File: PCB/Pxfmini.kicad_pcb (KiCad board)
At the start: 2 copper layers, 9 parts, among them P0 Raspberry pi GPIO, P1 MPU9250, P2 MS5611, P3 PCA9685, P4 PCA9685_2, P5 UART, P6 RC INPUT

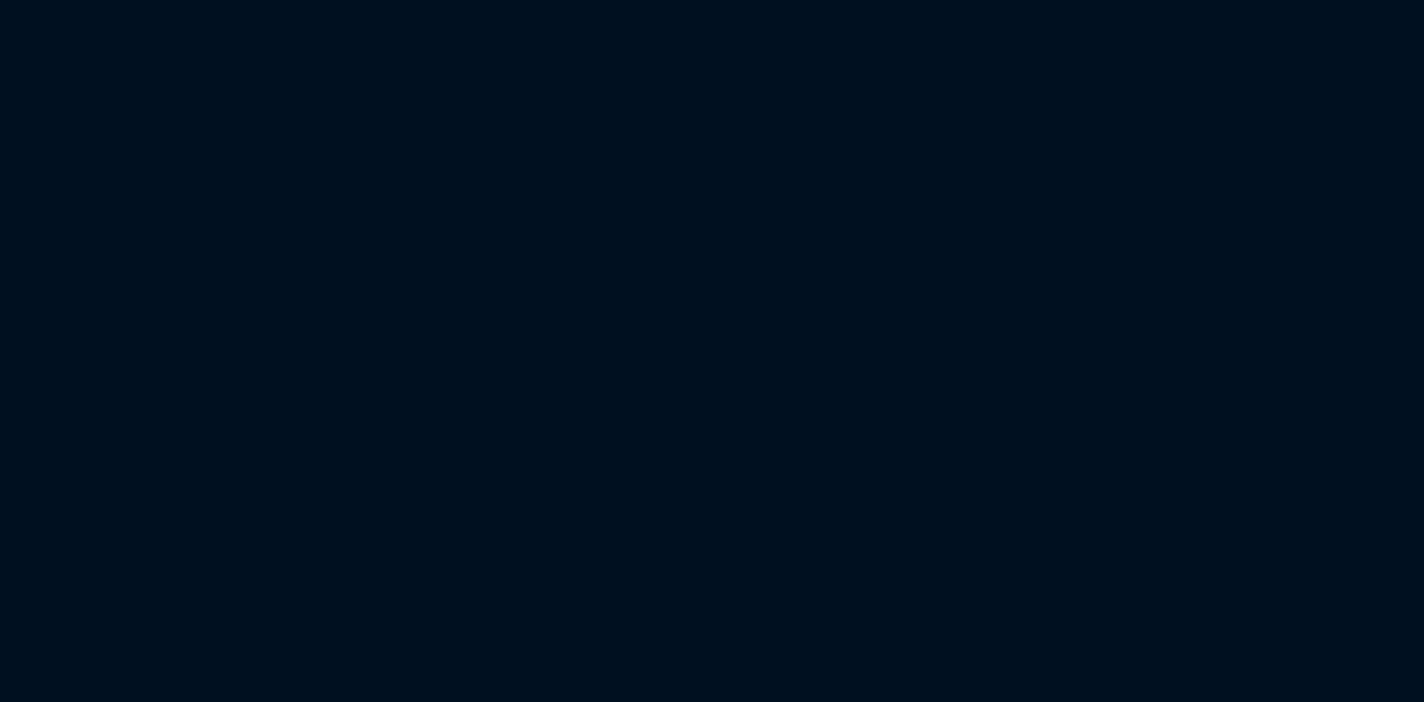
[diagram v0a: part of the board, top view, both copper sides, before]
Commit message: 
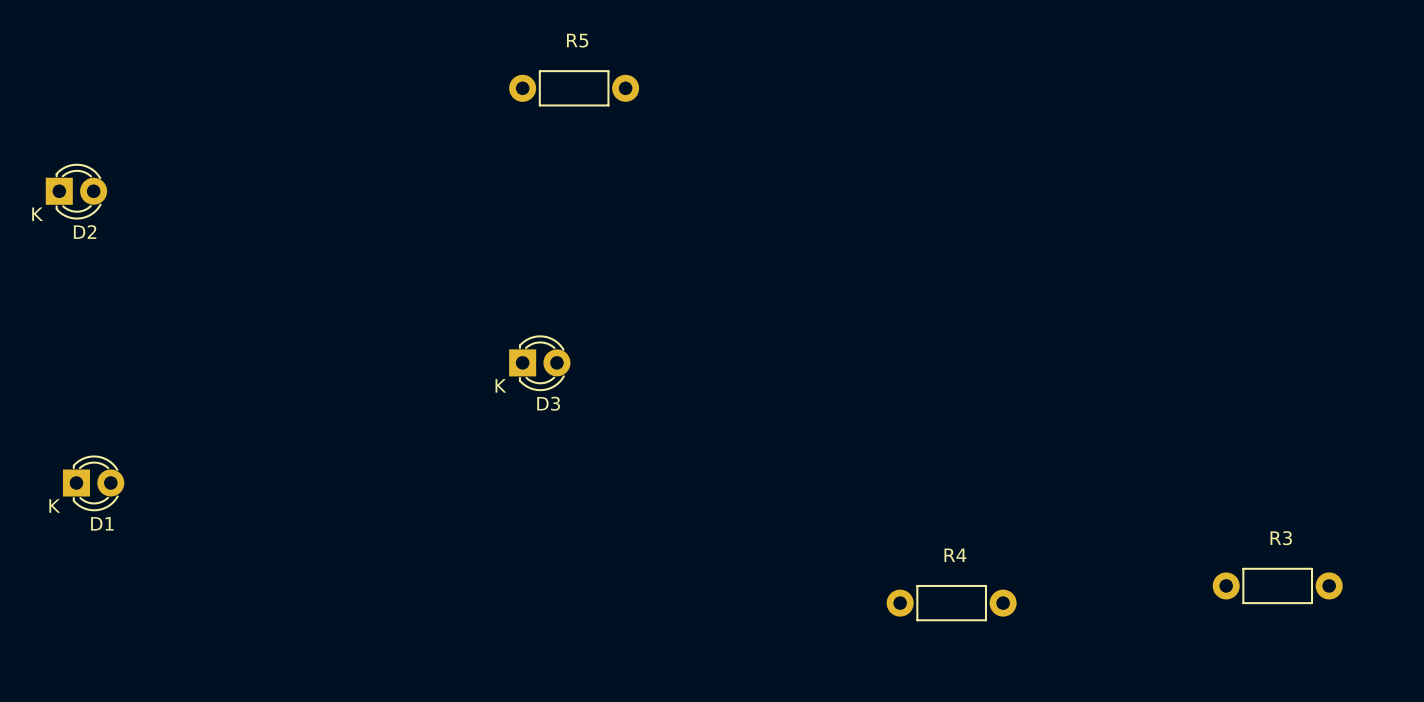
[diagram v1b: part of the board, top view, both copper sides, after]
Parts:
- added D1: LED_ARM, LEDs:LED-3MM, F.Cu at (67.3, 78.7)
- added D2: LED_CALIBRATION, LEDs:LED-3MM, F.Cu at (66.0, 57.1)
- added D3: LED_GPS, LEDs:LED-3MM, F.Cu at (100.3, 69.8)
- added R3: 220, Resistors_ThroughHole:Resistor_Horizontal_RM7mm, F.Cu at (152.4, 86.4)
- added R4: 220, Resistors_ThroughHole:Resistor_Horizontal_RM7mm, F.Cu at (128.3, 87.6)
- added R5: 220, Resistors_ThroughHole:Resistor_Horizontal_RM7mm, F.Cu at (100.3, 49.5)
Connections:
- P0 pad 18: Net-(P0-Pad18) -> /LED_ARM
- P0 pad 20: Net-(P0-Pad20) -> GND
- P0 pad 22: /CS_BARO -> /LED_CALIBRATION
- P0 pad 24: /CS_MPU -> /CS_BARO
- P0 pad 25: Net-(P0-Pad25) -> GND
- P0 pad 26: Net-(P0-Pad26) -> /CS_MPU
- P0 pad 36: Net-(P0-Pad36) -> /LED_GPS
- P0 pad 39: Net-(P0-Pad39) -> GND
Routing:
- net /CS_MPU: track 33.5 -> 7.62 mm
- net /CS_BARO: track 36.7 -> 61.3 mm
- net /LED_CALIBRATION: track 0.00 -> 1.27 mm

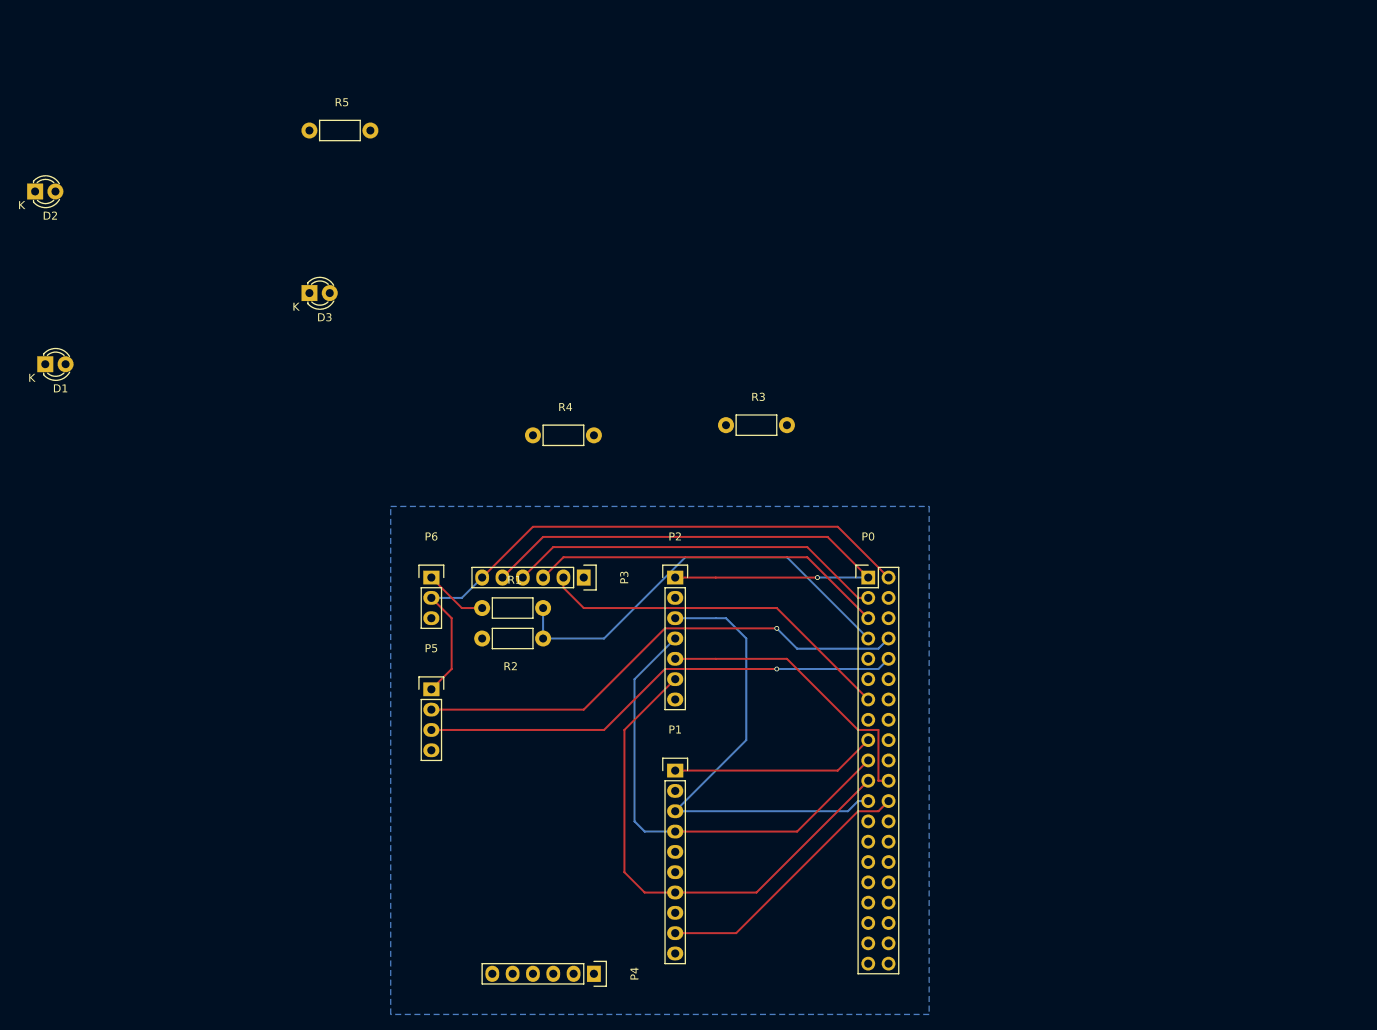
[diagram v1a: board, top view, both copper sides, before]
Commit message: 
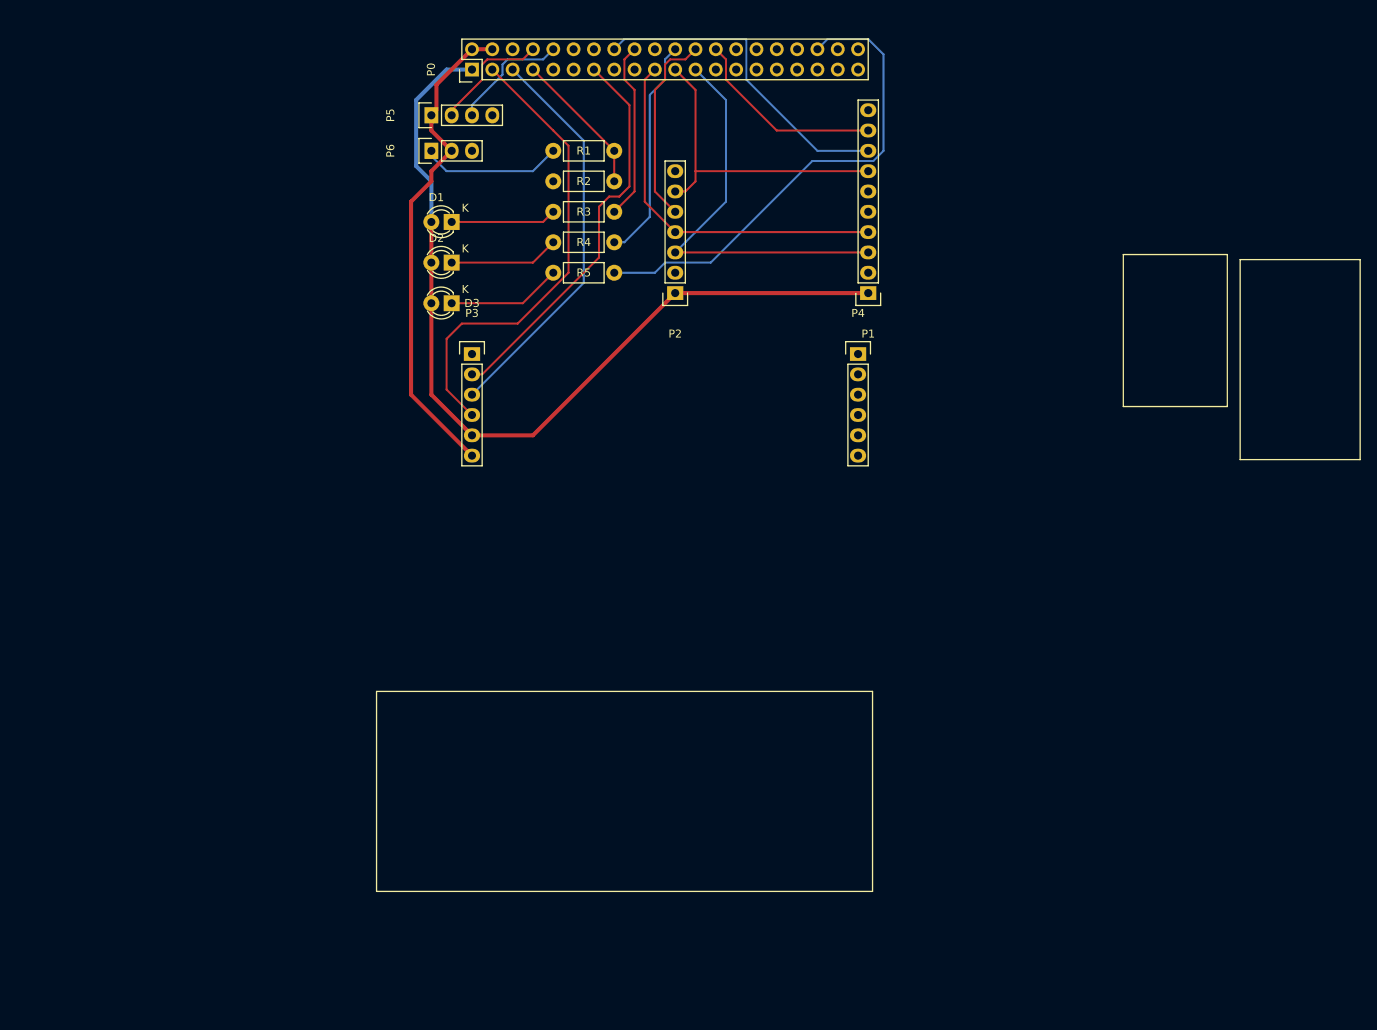
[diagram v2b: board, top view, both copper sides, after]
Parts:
- P0: value Raspberry pi GPIO -> Raspberry PI GPIO
- moved P4 84.2 mm to (168.9, 77.5), turned to 0 degrees
- moved P0 80.5 mm to (120.7, 41.9), turned to 90 degrees
- moved P5 71.8 mm to (115.6, 47.6), turned to 90 degrees
- moved P1 64.4 mm to (170.2, 69.8), turned to 180 degrees
- moved R1 57.8 mm to (130.8, 52.1)
- moved R2 57.8 mm to (138.4, 55.9)
- moved D1 53.8 mm to (118.1, 61.0), turned to 180 degrees
- moved P6 53.3 mm to (115.6, 52.1), turned to 90 degrees
- moved D2 52.8 mm to (118.1, 66.0), turned to 180 degrees
- moved P2 35.6 mm to (146.1, 69.8), turned to 180 degrees
- moved R5 35.3 mm to (130.8, 67.3)
- moved R3 34.3 mm to (130.8, 59.7)
- moved P3 31.2 mm to (120.7, 77.5), turned to 0 degrees
- moved R4 24.3 mm to (130.8, 63.5)
- moved D3 17.8 mm to (118.1, 71.1), turned to 180 degrees
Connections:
- P0 pad 14: Net-(P0-Pad14) -> GND
- P0 pad 16: Net-(P0-Pad16) -> /MPU_DRDY
- P0 pad 30: Net-(P0-Pad30) -> GND
- P0 pad 34: Net-(P0-Pad34) -> GND
- P1 pad 8: Net-(P1-Pad8) -> /MPU_DRDY
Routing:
- net /LED_GPS: track 0.00 -> 61.6 mm
- net /TXD: track 62.9 -> 15.1 mm, vias 1 -> 0
- net /RXD: track 60.8 -> 15.1 mm, vias 1 -> 0
- net /MPU_DRDY: track 0.00 -> 41.0 mm
- net /CS_BARO: track 61.3 -> 24.6 mm
- net /RC_INPUT: track 52.9 -> 18.2 mm
- net /LED_CALIBRATION: track 1.27 -> 28.0 mm
- net /MISO: track 64.1 -> 39.7 mm
- net /LED_ARM: track 0.00 -> 22.4 mm
- net /CS_MPU: track 7.62 -> 24.7 mm
- net +5V: track 77.0 -> 61.8 mm
- net Net-(D3-Pad1): track 0.00 -> 14.3 mm
- net Net-(D2-Pad1): track 0.00 -> 13.8 mm
- net Net-(D1-Pad1): track 0.00 -> 13.2 mm
- net /MOSI: track 58.4 -> 46.6 mm
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- removed copper zone on B.Cu, net GND
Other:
- net class Default: clearance 0.2 -> 0.2032; trace_width 0.25 -> 0.254
- net class Power added: clearance 0.2032, trace_width 0.508, via_dia 0.6, via_drill 0.4
- rule trace_clearance: 0.2 -> 0.2032

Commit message: 
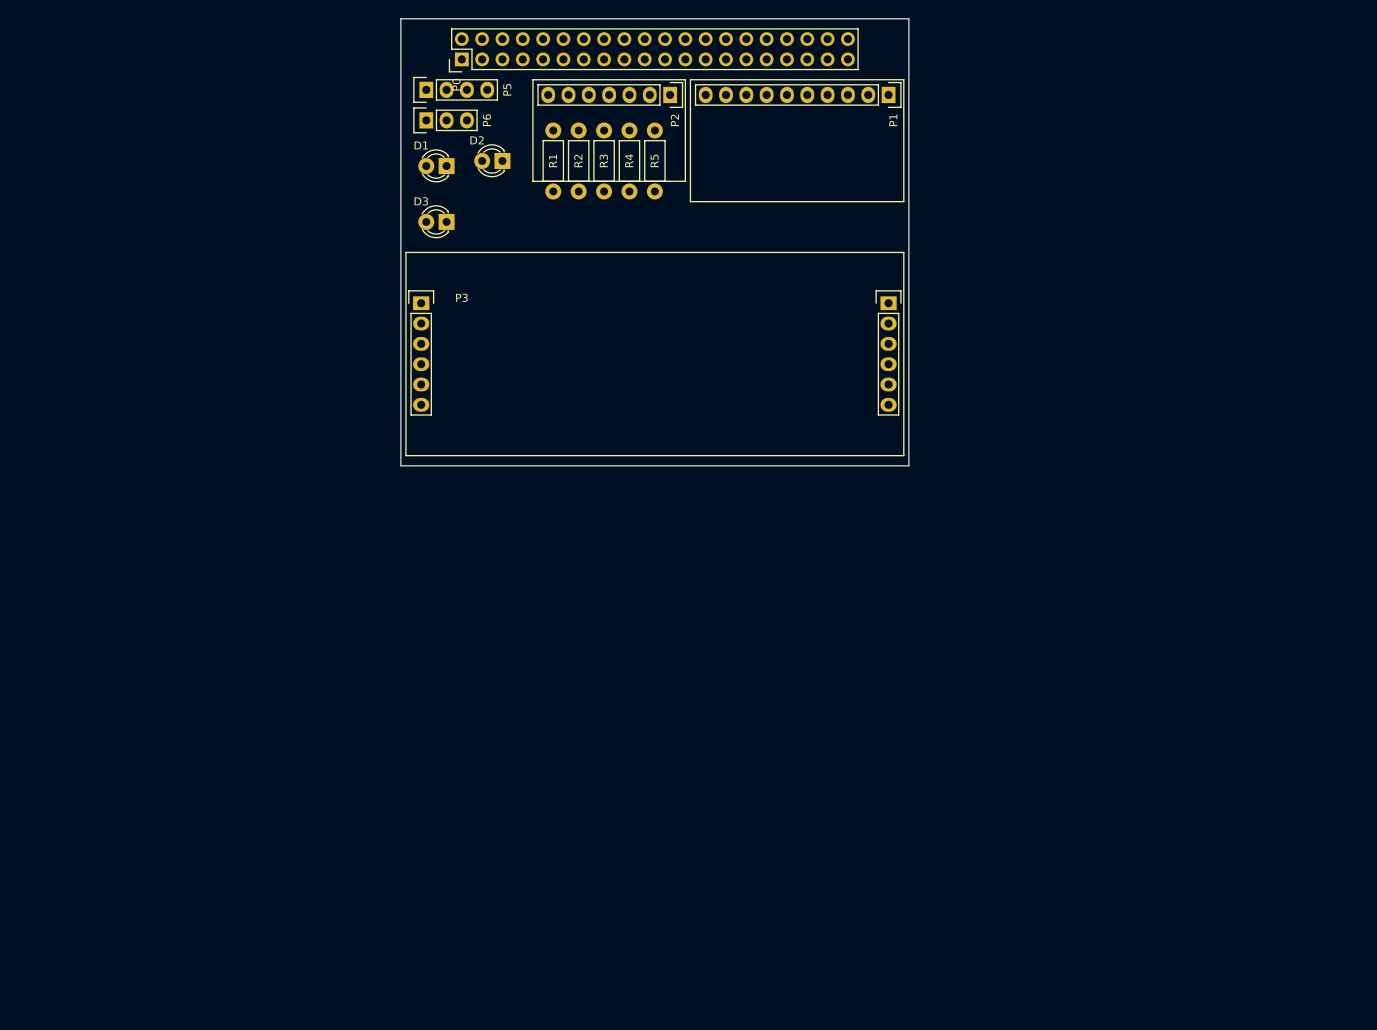
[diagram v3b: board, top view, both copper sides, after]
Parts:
- removed P4: PCA9685_2, Pin_Headers:Pin_Header_Straight_1x06
- P1: footprint Pin_Headers:Pin_Header_Straight_1x10 -> Raspmini:MPU9250
- P2: footprint Pin_Headers:Pin_Header_Straight_1x07 -> Raspmini:MS5611
- P3: footprint Pin_Headers:Pin_Header_Straight_1x06 -> Raspmini:PCA9685
- moved P1 24.9 mm to (172.7, 45.1), turned to 270 degrees
- moved P2 24.8 mm to (145.4, 45.1), turned to 270 degrees
- moved R5 16.3 mm to (143.5, 57.1), turned to 90 degrees
- moved D2 14.2 mm to (124.5, 53.3)
- moved P3 12.5 mm to (114.3, 66.7)
- moved R4 11.4 mm to (140.3, 57.1), turned to 90 degrees
- moved D3 10.2 mm to (117.5, 61.0)
- moved R2 7.75 mm to (134.0, 49.5), turned to 270 degrees
- moved D1 7.01 mm to (117.5, 54.0)
- moved R3 6.84 mm to (137.2, 57.1), turned to 90 degrees
- moved R1 5.08 mm to (130.8, 57.1), turned to 90 degrees
- moved P6 3.86 mm to (114.9, 48.3)
- moved P5 3.24 mm to (114.9, 44.5)
- moved P0 1.80 mm to (119.4, 40.6)
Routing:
- net +3V3: track 110.3 -> 0.00 mm
- net +5V: track 61.8 -> 0.00 mm
- net /LED_GPS: track 61.6 -> 0.00 mm
- net /SDA: track 58.8 -> 0.00 mm
- net /SCLK: track 51.2 -> 0.00 mm
- net /SCL: track 50.1 -> 0.00 mm
- net /EN_PWM: track 49.6 -> 0.00 mm
- net /MOSI: track 46.6 -> 0.00 mm
- net /MPU_DRDY: track 41.0 -> 0.00 mm
- net /MISO: track 39.7 -> 0.00 mm
- net /LED_CALIBRATION: track 28.0 -> 0.00 mm
- net /CS_MPU: track 24.7 -> 0.00 mm
- net /CS_BARO: track 24.6 -> 0.00 mm
- net /LED_ARM: track 22.4 -> 0.00 mm
- net /RC_INPUT: track 18.2 -> 0.00 mm
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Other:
- board outline added: 63.5 x 55.9 mm
- net class Default: clearance 0.2032 -> 0.254
- net class Power: clearance 0.2032 -> 0.254
- rule trace_clearance: 0.2032 -> 0.254

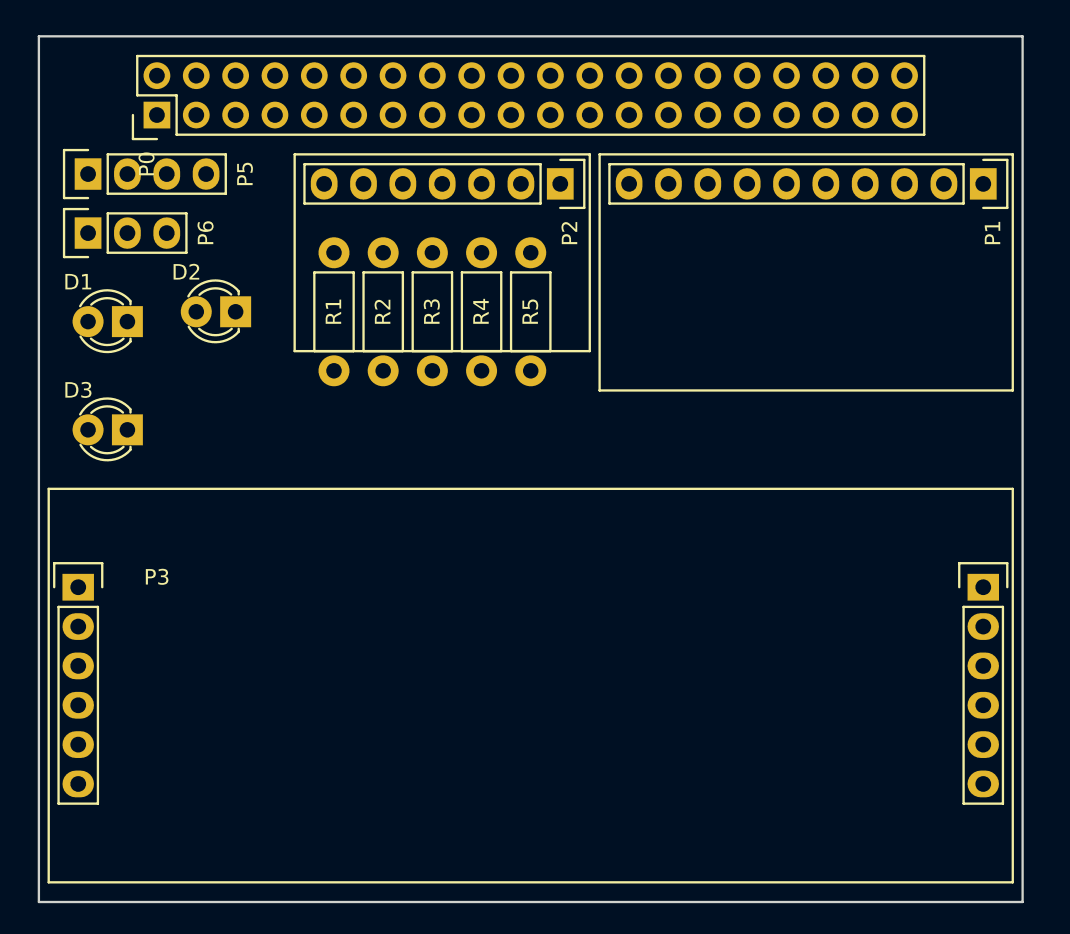
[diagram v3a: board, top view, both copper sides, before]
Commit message: 
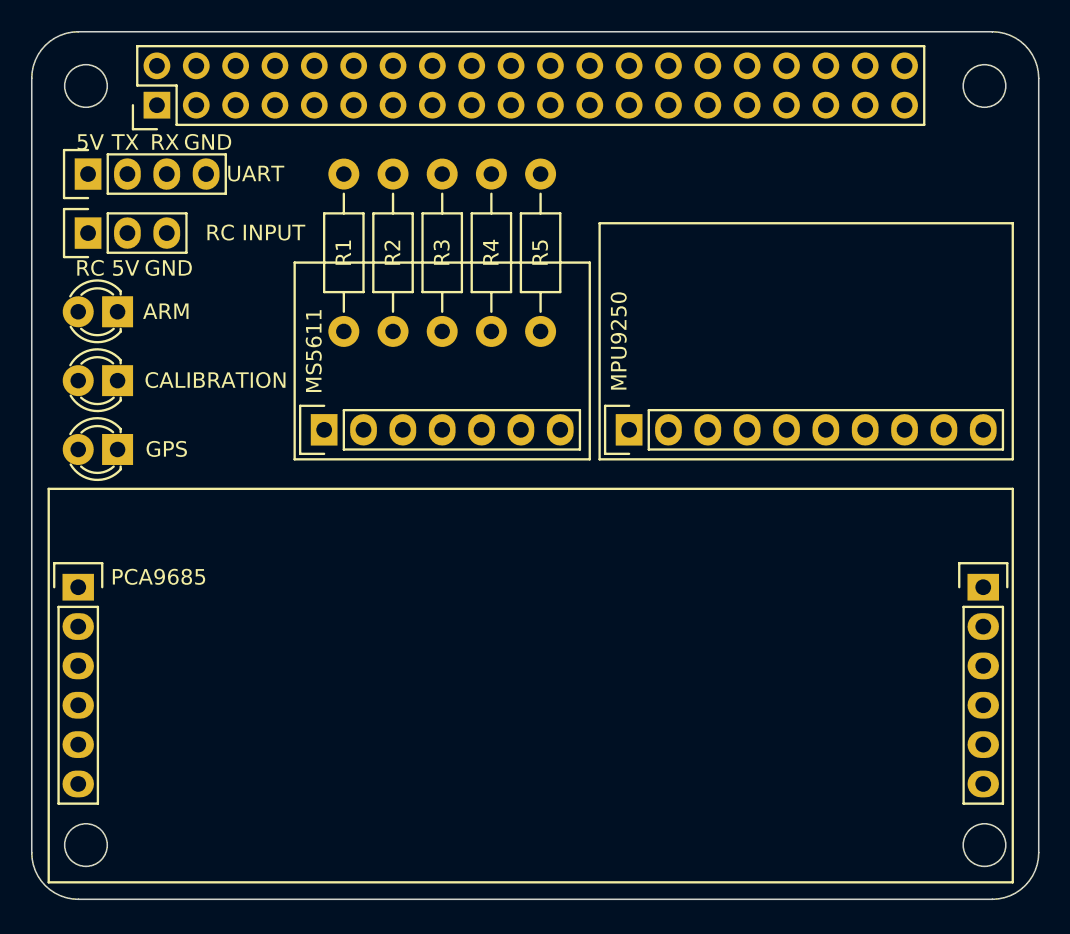
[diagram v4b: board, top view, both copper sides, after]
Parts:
- D1: value LED_ARM -> ARM
- D2: value LED_CALIBRATION -> CALIBRATION
- D3: value LED_GPS -> GPS
- R1, R2, R3, R4, R5: footprint Resistors_ThroughHole:Resistor_Horizontal_RM7mm -> Resistors_ThroughHole:Resistor_Horizontal_RM10mm
- moved P1 27.8 mm to (149.9, 61.0), turned to 90 degrees
- moved P2 22.0 mm to (130.2, 61.0), turned to 90 degrees
- moved D2 8.82 mm to (116.8, 57.8)
- moved R2 5.12 mm to (134.6, 44.5)
- moved R5 2.62 mm to (144.1, 54.6)
- moved R1 2.62 mm to (131.4, 54.6)
- moved R3 2.62 mm to (137.8, 54.6)
- moved R4 2.62 mm to (141.0, 54.6)
- moved D3 1.42 mm to (116.8, 62.2)
- moved D1 0.90 mm to (116.8, 53.3)
- moved P0 0.63 mm to (119.4, 40.0)
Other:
- board size 63.5 x 55.9 mm -> 65 x 56 mm
- board text added: "5V"
- board text added: "GND"
- board text added: "RC"
- board text added: "RX"
- board text added: "TX"
